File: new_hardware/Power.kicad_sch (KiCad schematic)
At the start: 40 parts, among them SW1 GT-TC054A-H035-L1, U3 AXP2101, U4 SGM6603-ADJYN6G, U5 SGM3204

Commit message: some changes
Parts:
- L1, L2: value 4.7u -> 1u; Manufacturer (none) -> Murata; Mnfct.  partnumber (none) -> LQM2MPN1R0NG0L
- R1, R14, R2, R4, R5, R6: footprint (none) -> rlib_passive:R_0603_1608Metric

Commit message: xxxx
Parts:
- removed L4: 2.2u, rlib_passive:IND_LQH32PN4R7NN0L, symbol rlib_passive:L
- removed TP4: TestPoint, symbol Connector:TestPoint
- added L6: L, rlib_passive:INDC2520X120N, symbol rlib_passive:L
- added R49, R50: 0, rlib_passive:R_0603_1608Metric, symbol rlib_passive:R
- C61: renamed from C1; value 10u -> 1u; footprint (none) -> rlib_passive:C_0603_1608Metric
- C62: renamed from C2; footprint (none) -> rlib_passive:C_0603_1608Metric
- C63: renamed from C3; footprint (none) -> rlib_passive:C_0603_1608Metric
- C64: renamed from C4; footprint (none) -> rlib_passive:C_0603_1608Metric
- C65: renamed from C5; footprint (none) -> rlib_passive:C_0603_1608Metric
- C66: renamed from C6; footprint (none) -> rlib_passive:C_0603_1608Metric
- C67: renamed from C7; footprint (none) -> rlib_passive:C_0603_1608Metric
- C68: renamed from C8; footprint (none) -> rlib_passive:C_0603_1608Metric
- C69: renamed from C9; footprint (none) -> rlib_passive:C_0603_1608Metric
- C70: renamed from C10; footprint (none) -> rlib_passive:C_0603_1608Metric
- C71: renamed from C11; footprint (none) -> rlib_passive:C_0603_1608Metric
- C72: renamed from C12; footprint (none) -> rlib_passive:C_0603_1608Metric
- C73: renamed from C13; footprint (none) -> rlib_passive:C_0603_1608Metric
- C74: renamed from C14; footprint (none) -> rlib_passive:C_0603_1608Metric
- C75: renamed from C16; footprint (none) -> rlib_passive:C_0603_1608Metric
- L2: renamed from L1; footprint rlib_passive:IND_LQH32PN4R7NN0L -> rlib_passive:INDC2016X100N
- L3: renamed from L2; footprint rlib_passive:IND_LQH32PN4R7NN0L -> rlib_passive:INDC2016X100N
- L5: value 2.2u -> L; footprint rlib_passive:IND_LQH32PN4R7NN0L -> rlib_passive:INDC2520X120N; LCSC partnumber (none) -> C85840; Mnfct.  partnumber (none) -> BLM21PG221SN1D
- R44: renamed from R4; value 1k -> 10k
- TP15: renamed from TP1; footprint (none) -> TestPoint:TestPoint_Pad_D1.0mm
- TP16: renamed from TP2; footprint (none) -> TestPoint:TestPoint_Pad_D1.0mm
- TP17: renamed from TP3; footprint (none) -> TestPoint:TestPoint_Pad_D1.0mm
- TP19: renamed from TP5; footprint (none) -> TestPoint:TestPoint_Pad_D1.0mm
- TP20: renamed from TP7; footprint (none) -> TestPoint:TestPoint_Pad_D1.0mm
- U9: renamed from U3; footprint axp2101:QFN-40_L5.0-W5.0-P0.40-TL-EP3.4 -> rlib_power:QFN-40_L5.0-W5.0-P0.40-TL-EP3.4
- renumbered D1 to D11, D2 to D12, F1 to F2, L3 to L4, R1 to R43, R2 to R45, R14 to R46, R5 to R47, R6 to R48, SW1 to SW8, U4 to U10, U5 to U11
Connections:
- net +5VA: now also L6.2; no longer L5.2
- net -5VA: now also L5.2
- net VCC: now also R49.2, R50.2; no longer U9.13 (BLDOIN), U9.17 (ALDOIN)
- net at C72.1, U11.1 (OUT): now also L5.1
- net at C73.1, R47.2, U10.5 (VOUT): now also L6.1; no longer L5.1
- new net: R50.1, U9.13 (BLDOIN)
- new net: R49.1, U9.17 (ALDOIN)
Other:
- moved on the sheet: C61, C66, C69, C73, C75, D11, D12, F2, NT1, R44, SW8, TP15

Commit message: changed lcd interface and layout is partly made
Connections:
- net +3V3: no longer C65.1, L3.2, TP17.1, U9.26 (FB2)
- new net +0V9: C65.1, L3.2, TP17.1, U9.26 (FB2)
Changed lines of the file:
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@@
   (symbol (lib_id "rlib_power:+0V9") (at 139.7 66.04 270) (unit 1)
     (in_bom yes) (on_board yes) (fields_autoplaced)
-    (property "Reference" "#PWR0112" (id 0) (at 135.89 66.04 0)
+    (property "Reference" "#PWR0136" (id 0) (at 135.89 66.04 0)
       (effects (font (size 1.27 1.27)) hide)
     )

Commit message: some fucking changes
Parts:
- removed C66: 10u, rlib_passive:C_0603_1608Metric, symbol rlib_passive:C
- removed L5, L6: L, rlib_passive:INDC2520X120N, symbol rlib_passive:L
- added FB2, FB3: FerriteBead, rlib_passive:INDC2520X120N, symbol rlib_passive:FerriteBead
- added R54, R55: 0, rlib_passive:R_0603_1608Metric, symbol rlib_passive:R
- C61, C63: LCSC partnumber (none) -> C77386; Manufacturer (none) -> Murata; Mnfct. partnumber (none) -> GRM188R61H105KAALD
- C62: LCSC partnumber (none) -> C91606; Manufacturer (none) -> Murata; Mnfct. partnumber (none) -> GRM188R61E106MA73D
- C64, C65: LCSC partnumber (none) -> C126630; Manufacturer (none) -> Murata; Mnfct. partnumber (none) -> GRT188R61A226ME13D
- C67, C68, C69, C70, C72, C73, C74, C75: LCSC Partnumber C91606 -> (none); LCSC partnumber (none) -> C91606
- D11: LCSC partnumber (none) -> C2845380; Manufacturer (none) -> HCTL; Mnfct. partnumber (none) -> HC-1.25-3PWT
- D12: LCSC partnumber (none) -> C2827682; Manufacturer (none) -> TECH PUBLIC; Mnfct. partnumber (none) -> PESD3V3L1BA
- NT1: footprint (none) -> NetTie:NetTie-2_SMD_Pad2.0mm
- R43, R45: LCSC partnumber (none) -> C218056; Manufacturer (none) -> Viking Tech; Mnfct. partnumber (none) -> ARG03FTC4701; Tolerance (none) -> 1%
- R44, R46: LCSC partnumber (none) -> C217687; Manufacturer (none) -> Viking Tech; Mnfct. partnumber (none) -> ARG03FTC1002; Tolerance (none) -> 1%
- R47: value R -> 100k; LCSC partnumber (none) -> C217682; Manufacturer (none) -> Viking Tech; Mnfct. partnumber (none) -> ARG03FTC1003; Tolerance (none) -> 1%
- R48: value R -> 11k; LCSC partnumber (none) -> C217703; Manufacturer (none) -> Viking Tech; Mnfct. partnumber (none) -> ARG03FTC1102; Tolerance (none) -> 1%
- SW8: LCSC partnumber (none) -> C778158
- TP16, TP17, TP19, TP20: now left out of the parts list
- U11: LCSC partnumber C194031 -> C45000
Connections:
- net +5VA: now also FB3.2
- net -5VA: now also FB2.2
- net GND: now also R54.1, R55.1
- net at C72.1, U11.1 (OUT): now also FB2.1
- net VBUS: now reaches C62.1, U9.37 (VBUS)
- net at U9.6 (VIN3): now also R54.2
- net at U9.7 (VIN4): now also R55.2
- net at C73.1, R47.2, U10.5 (VOUT): now also FB3.1

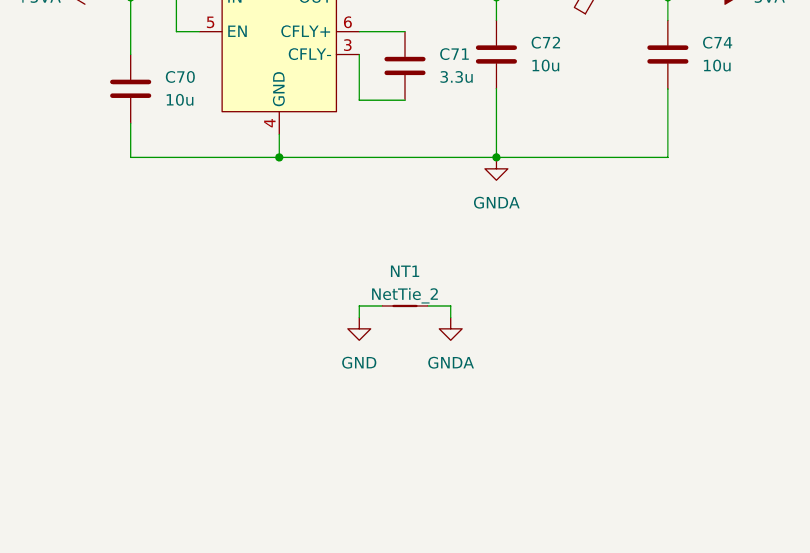
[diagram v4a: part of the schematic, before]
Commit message: device tree is changed
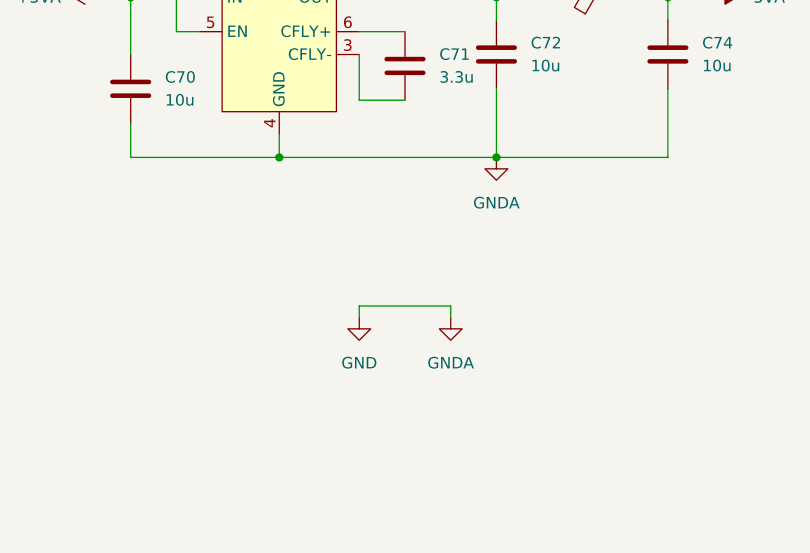
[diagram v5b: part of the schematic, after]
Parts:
- removed NT1: NetTie_2, NetTie:NetTie-2_SMD_Pad2.0mm, symbol Device:NetTie_2
- R49, R50, R54, R55: LCSC partnumber (none) -> C465460; Manufacturer (none) -> Viking Tech; Mnfct. partnumber (none) -> CR-03JA7----0R
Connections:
- net GNDA is gone; now on net GND: C69.2, C70.2, C72.2, C73.2, C74.2, C75.2, R48.1, U10.2 (GND), U11.4 (GND)
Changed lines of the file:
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@@
-    (stroke (width 0) (type default) (color 0 0 0 0))
-  )
-  (wire (pts (xy 226.06 125.73) (xy 228.6 125.73))
     (stroke (width 0) (type default) (color 0 0 0 0))
   )
@@
     (stroke (width 0) (type default) (color 0 0 0 0))
   )
-  (wire (pts (xy 233.68 125.73) (xy 236.22 125.73))
+  (wire (pts (xy 226.06 125.73) (xy 236.22 125.73))
     (stroke (width 0) (type default) (color 0 0 0 0))
   )
@@
       (effects (font (size 1.27 1.27)) hide)
     )
-    (property "Manufacturer" "" (id 5) (at 128.27 96.52 0)
+    (property "Manufacturer" "Viking Tech" (id 5) (at 128.27 96.52 0)
       (effects (font (size 1.27 1.27)) hide)
     )
@@
       (effects (font (size 1.27 1.27)) hide)
     )
-    (property "LCSC partnumber" "" (id 9) (at 128.27 96.52 0)
-      (effects (font (size 1.27 1.27)) hide)
-    )
-    (property "Mnfct. partnumber" "" (id 10) (at 128.27 96.52 0)
+    (property "LCSC partnumber" "C465460" (id 9) (at 128.27 96.52 0)
+      (effects (font (size 1.27 1.27)) hide)
+    )
+    (property "Mnfct. partnumber" "CR-03JA7----0R " (id 10) (at 128.27 96.52 0)
       (effects (font (size 1.27 1.27)) hide)
     )
@@
     (pin "1")
   )
-  (symbol (lib_id "Device:NetTie_2") (at 231.14 125.73 0) (unit 1)
-    (in_bom yes) (on_board yes)
-    (property "Reference" "NT1" (id 0) (at 231.14 121.92 0))
-    (property "Value" "NetTie_2" (id 1) (at 231.14 124.46 0))
-    (property "Footprint" "NetTie:NetTie-2_SMD_Pad2.0mm" (id 2) (at 231.14 125.73 0)
-      (effects (font (size 1.27 1.27)) hide)
-    )
-    (property "Datasheet" "~" (id 3) (at 231.14 125.73 0)
-      (effects (font (size 1.27 1.27)) hide)
-    )
-    (pin "1")
-    (pin "2")
-  )
   (symbol (lib_id "rlib_power:+0V9") (at 139.7 66.04 270) (unit 1)
     (in_bom yes) (on_board yes) (fields_autoplaced)
@@
       (effects (font (size 1.27 1.27)) hide)
     )
-    (property "Manufacturer" "" (id 5) (at 71.12 69.85 0)
+    (property "Manufacturer" "Viking Tech" (id 5) (at 71.12 69.85 0)
       (effects (font (size 1.27 1.27)) hide)
     )
@@
       (effects (font (size 1.27 1.27)) hide)
     )
-    (property "LCSC partnumber" "" (id 9) (at 71.12 69.85 0)
-      (effects (font (size 1.27 1.27)) hide)
-    )
-    (property "Mnfct. partnumber" "" (id 10) (at 71.12 69.85 0)
+    (property "LCSC partnumber" "C465460" (id 9) (at 71.12 69.85 0)
+      (effects (font (size 1.27 1.27)) hide)
+    )
+    (property "Mnfct. partnumber" "CR-03JA7----0R " (id 10) (at 71.12 69.85 0)
       (effects (font (size 1.27 1.27)) hide)
     )
@@
       (effects (font (size 1.27 1.27)) hide)
     )
-    (property "Manufacturer" "" (id 5) (at 128.27 78.74 0)
+    (property "Manufacturer" "Viking Tech" (id 5) (at 128.27 78.74 0)
       (effects (font (size 1.27 1.27)) hide)
     )
@@
       (effects (font (size 1.27 1.27)) hide)
     )
-    (property "LCSC partnumber" "" (id 9) (at 128.27 78.74 0)
-      (effects (font (size 1.27 1.27)) hide)
-    )
-    (property "Mnfct. partnumber" "" (id 10) (at 128.27 78.74 0)
+    (property "LCSC partnumber" "C465460" (id 9) (at 128.27 78.74 0)
+      (effects (font (size 1.27 1.27)) hide)
+    )
+    (property "Mnfct. partnumber" "CR-03JA7----0R " (id 10) (at 128.27 78.74 0)
       (effects (font (size 1.27 1.27)) hide)
     )
@@
       (effects (font (size 1.27 1.27)) hide)
     )
-    (property "Manufacturer" "" (id 5) (at 71.12 78.74 0)
+    (property "Manufacturer" "Viking Tech" (id 5) (at 71.12 78.74 0)
       (effects (font (size 1.27 1.27)) hide)
     )
@@
       (effects (font (size 1.27 1.27)) hide)
     )
-    (property "LCSC partnumber" "" (id 9) (at 71.12 78.74 0)
-      (effects (font (size 1.27 1.27)) hide)
-    )
-    (property "Mnfct. partnumber" "" (id 10) (at 71.12 78.74 0)
-      (effects (font (size 1.27 1.27)) hide)
-    )
+    (property "LCSC partnumber" "C465460" (id 9) (at 71.12 78.74 0)
+      (effects (font (size 1.27 1.27)) hide)
+    )
+    (property "Mnfct. partnumber" "CR-03JA7----0R " (id 10) (at 71.12 78.74 0)
+      (effects (font (size 1.27 1.27)) hide)
+    )

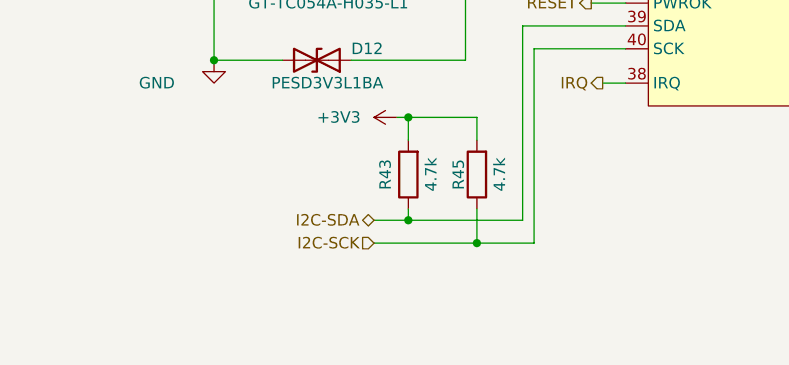
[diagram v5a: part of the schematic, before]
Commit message: wi-fi module is moved to closer board outline,unused files are removed
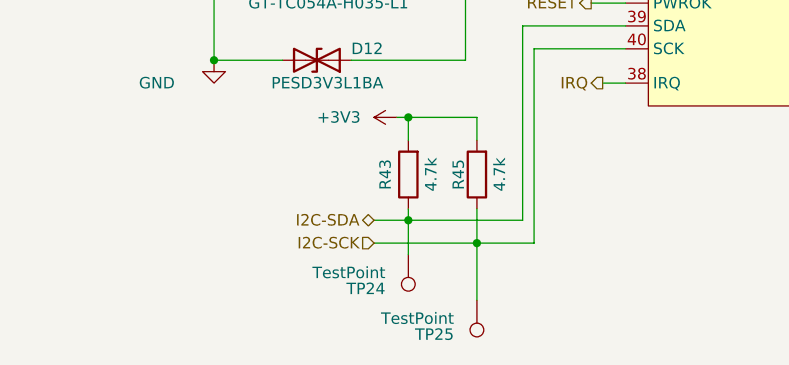
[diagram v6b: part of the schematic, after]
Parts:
- added TP24, TP25: TestPoint, TestPoint:TestPoint_Pad_D1.0mm, symbol Connector:TestPoint
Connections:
- net I2C-SCK: now also TP25.1
- net I2C-SDA: now also TP24.1
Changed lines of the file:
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@@
+    (stroke (width 0) (type default) (color 0 0 0 0))
+  )
+  (wire (pts (xy 57.15 147.32) (xy 57.15 151.13))
     (stroke (width 0) (type default) (color 0 0 0 0))
   )
@@
   )
   (wire (pts (xy 123.19 78.74) (xy 124.46 78.74))
+    (stroke (width 0) (type default) (color 0 0 0 0))
+  )
+  (wire (pts (xy 64.77 149.86) (xy 64.77 156.21))
     (stroke (width 0) (type default) (color 0 0 0 0))
   )
@@
     (pin "2")
   )
+  (symbol (lib_id "Connector:TestPoint") (at 64.77 156.21 180) (unit 1)
+    (in_bom no) (on_board yes)
+    (property "Reference" "TP25" (id 0) (at 62.23 160.02 0)
+      (effects (font (size 1.27 1.27)) (justify left))
+    )
+    (property "Value" "TestPoint" (id 1) (at 62.23 158.2421 0)
+      (effects (font (size 1.27 1.27)) (justify left))
+    )
+    (property "Footprint" "TestPoint:TestPoint_Pad_D1.0mm" (id 2) (at 59.69 156.21 0)
+      (effects (font (size 1.27 1.27)) hide)
+    )
+    (property "Datasheet" "~" (id 3) (at 59.69 156.21 0)
+      (effects (font (size 1.27 1.27)) hide)
+    )
+    (pin "1")
+  )
   (symbol (lib_id "rlib_passive:R") (at 128.27 78.74 270) (unit 1)
     (in_bom yes) (on_board yes)
@@
     (pin "2")
   )
+  (symbol (lib_id "Connector:TestPoint") (at 57.15 151.13 180) (unit 1)
+    (in_bom no) (on_board yes)
+    (property "Reference" "TP24" (id 0) (at 54.61 154.94 0)
+      (effects (font (size 1.27 1.27)) (justify left))
+    )
+    (property "Value" "TestPoint" (id 1) (at 54.61 153.1621 0)
+      (effects (font (size 1.27 1.27)) (justify left))
+    )
+    (property "Footprint" "TestPoint:TestPoint_Pad_D1.0mm" (id 2) (at 52.07 151.13 0)
+      (effects (font (size 1.27 1.27)) hide)
+    )
+    (property "Datasheet" "~" (id 3) (at 52.07 151.13 0)
+      (effects (font (size 1.27 1.27)) hide)
+    )
+    (pin "1")
+  )
   (symbol (lib_id "rlib_passive:C") (at 135.89 52.07 0) (unit 1)
